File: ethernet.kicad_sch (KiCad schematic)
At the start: 41 parts, among them J10 J3011G21DNL, U3 LFSPXO025560REEL, U4 LAN8740A-EN

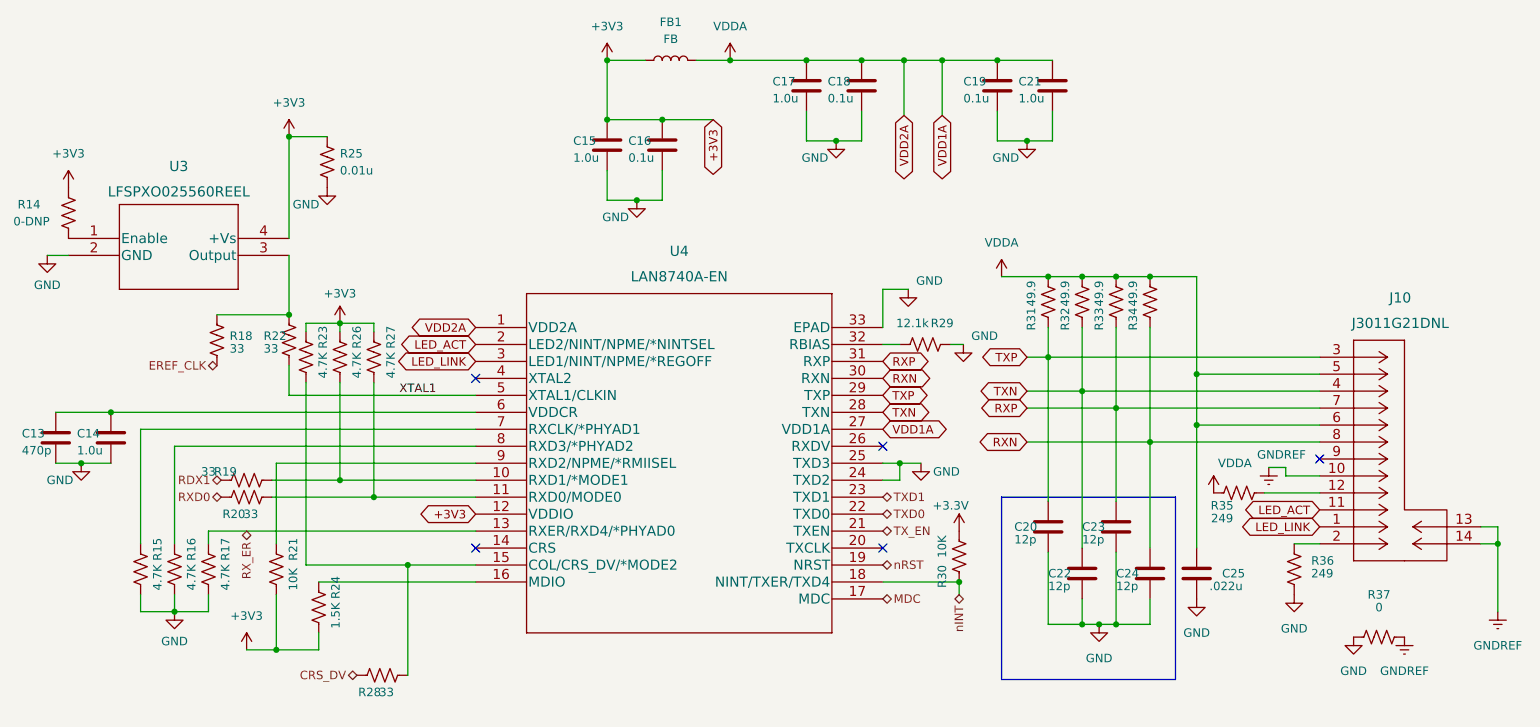
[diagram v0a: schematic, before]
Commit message: Imported AISLER 2Layer-Complex design rules Added Silkscreen to all passives to help with orientation Moved C15 and C16 to the back in order to be physically closer to the VDDIO pin of the LAN8740a Increased trace width of some 5v traces to the proper 0.5mm
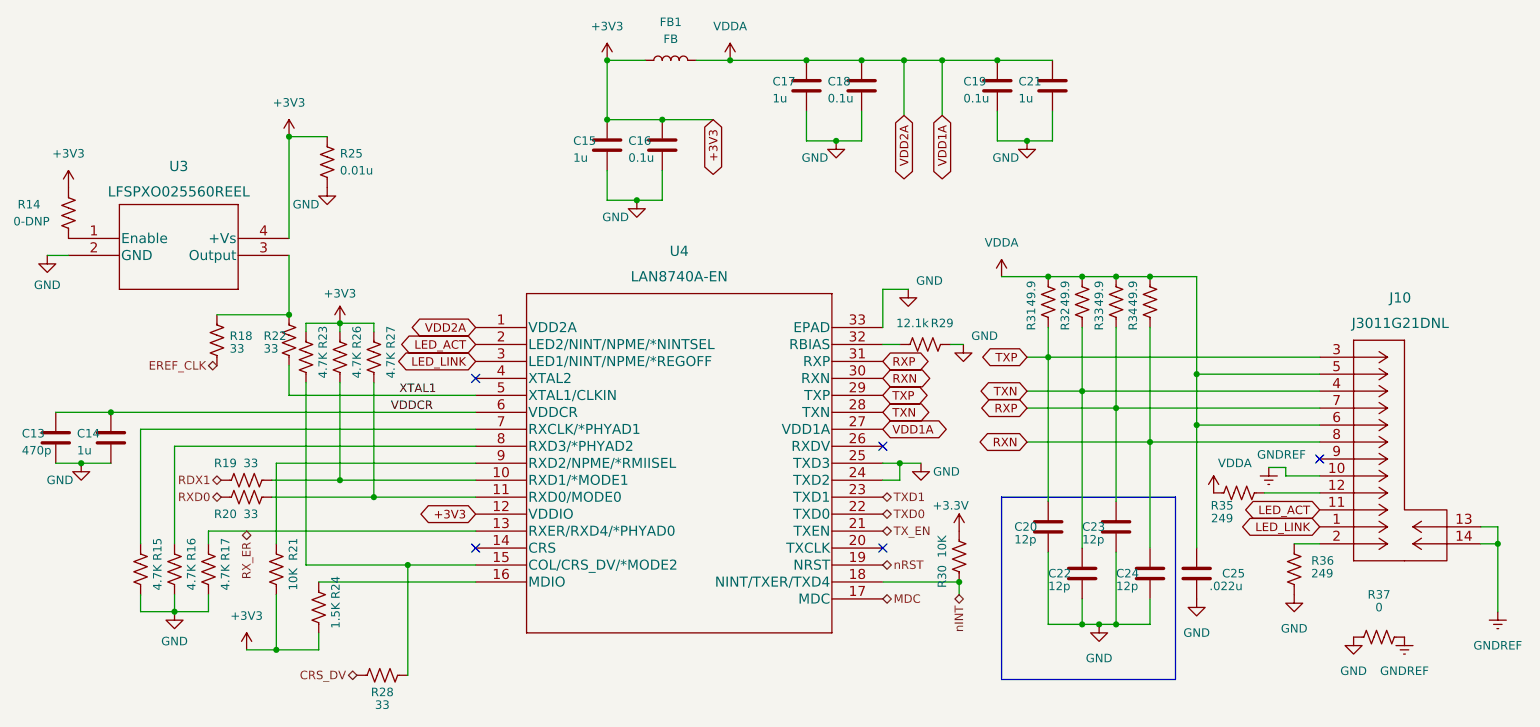
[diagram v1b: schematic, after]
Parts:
- C14, C15, C17, C21: value 1.0u -> 1u
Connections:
- net VDDCR: now reaches C13.1, C14.1, U4.6 (VDDCR)
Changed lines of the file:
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@@
     (stroke (width 0) (type default) (color 0 0 0 0))
+  )
+  (label "VDDCR" (at 80.01 85.09 0)
+    (effects (font (size 1.27 1.27)) (justify left bottom))
   )
   (label "XTAL1" (at 81.28 82.55 0)
@@
   (symbol (lib_id "Device:R_US") (at 58.42 97.79 270) (unit 1)
     (in_bom yes) (on_board yes)
-    (property "Reference" "R20" (id 0) (at 56.515 100.33 90))
+    (property "Reference" "R20" (id 0) (at 55.245 100.33 90))
     (property "Value" "33" (id 1) (at 59.055 100.33 90))
     (property "Footprint" "Lambley:0603-1608M" (id 2) (at 58.166 98.806 90)
@@
   (symbol (lib_id "Device:R_US") (at 58.42 95.25 270) (unit 1)
     (in_bom yes) (on_board yes)
-    (property "Reference" "R19" (id 0) (at 55.245 93.98 90))
-    (property "Value" "33" (id 1) (at 52.705 93.98 90))
+    (property "Reference" "R19" (id 0) (at 55.245 92.71 90))
+    (property "Value" "33" (id 1) (at 59.055 92.71 90))
     (property "Footprint" "Lambley:0603-1608M" (id 2) (at 58.166 96.266 90)
       (effects (font (size 1.27 1.27)) hide)
@@
       (effects (font (size 1.27 1.27)) (justify left))
     )
-    (property "Value" "1.0u" (id 1) (at 107.315 46.99 0)
+    (property "Value" "1u" (id 1) (at 107.315 46.99 0)
       (effects (font (size 1.27 1.27)) (justify left))
     )
@@
       (effects (font (size 1.27 1.27)) (justify left))
     )
-    (property "Value" "1.0u" (id 1) (at 137.16 38.1 0)
+    (property "Value" "1u" (id 1) (at 137.16 38.1 0)
       (effects (font (size 1.27 1.27)) (justify left))
     )
@@
       (effects (font (size 1.27 1.27)) (justify left))
     )
-    (property "Value" "1.0u" (id 1) (at 33.02 90.805 0)
+    (property "Value" "1u" (id 1) (at 33.02 90.805 0)
       (effects (font (size 1.27 1.27)) (justify left))
     )
@@
   (symbol (lib_id "Device:R_US") (at 78.74 124.46 270) (unit 1)
     (in_bom yes) (on_board yes)
-    (property "Reference" "R28" (id 0) (at 76.835 127 90))
-    (property "Value" "33" (id 1) (at 79.375 127 90))
+    (property "Reference" "R28" (id 0) (at 78.74 127 90))
+    (property "Value" "33" (id 1) (at 78.74 128.905 90))
     (property "Footprint" "Lambley:0603-1608M" (id 2) (at 78.486 125.476 90)
       (effects (font (size 1.27 1.27)) hide)
@@
       (effects (font (size 1.27 1.27)) (justify left))
     )
-    (property "Value" "1.0u" (id 1) (at 173.99 38.1 0)
-      (effects (font (size 1.27 1.27)) (justify left))
-    )
+    (property "Value" "1u" (id 1) (at 173.99 38.1 0)
+      (effects (font (size 1.27 1.27)) (justify left))
+    )

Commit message: Fixed nINT not actually being connected to 3v3 Changed the pic32MX7* 100 pin footprint from the T package to the F package Added some silkscreen around the DIGITAL and ANALOG headers
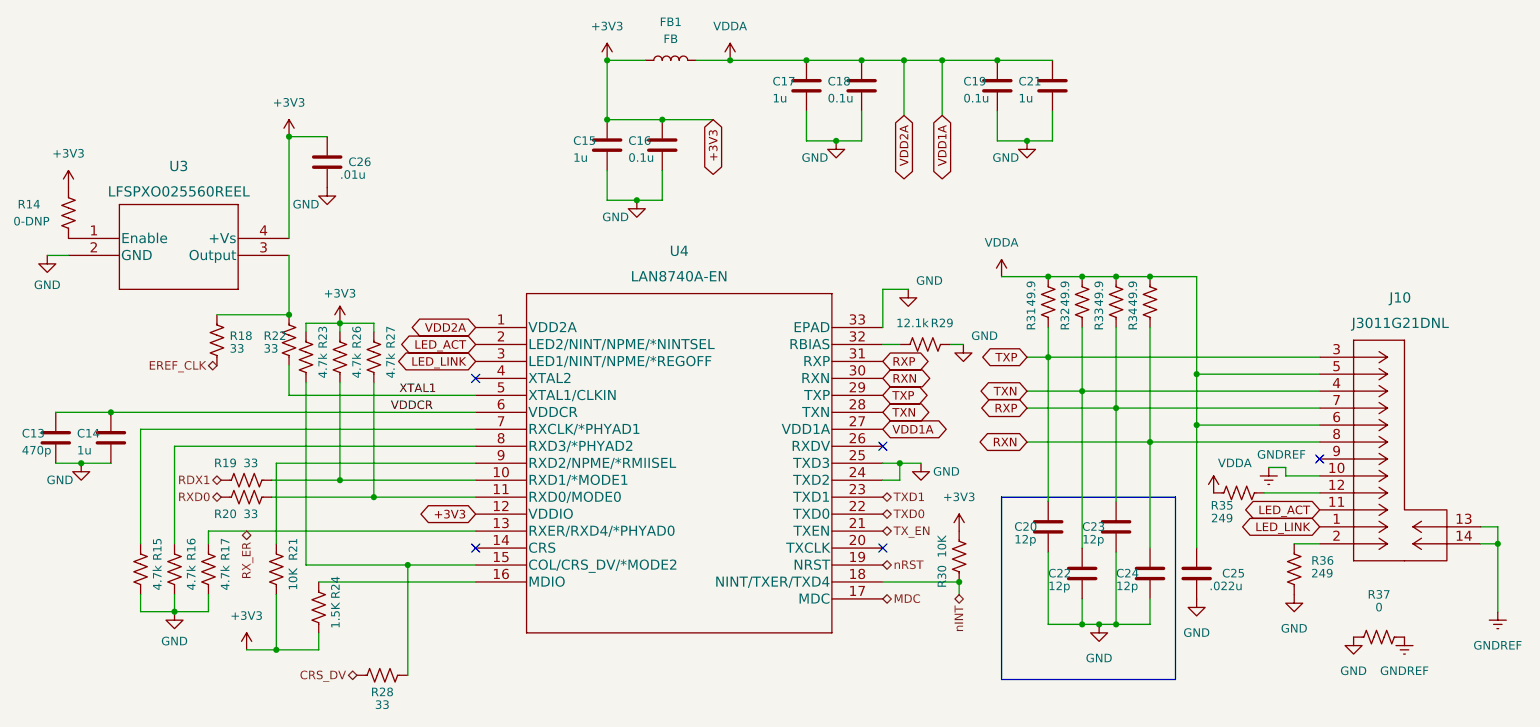
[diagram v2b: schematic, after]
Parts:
- removed R25: 0.01u, Lambley:0603-1608M, symbol Device:R_US
- added C26: .01u, Lambley:0603-1608M, symbol Device:C
- R15, R16, R17, R23, R26, R27: value 4.7K -> 4.7k
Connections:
- net +3.3V is gone; now on net +3V3: R30.1
- net +3V3: now also C26.1
- net GND: now also C26.2
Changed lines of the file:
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@@
     (pin "2")
-  )
-  (symbol (lib_id "power:+3.3V") (at 165.1 102.87 0) (unit 1)
-    (in_bom yes) (on_board yes)
-    (property "Reference" "#PWR0158" (id 0) (at 165.1 106.68 0)
-      (effects (font (size 1.27 1.27)) hide)
-    )
-    (property "Value" "+3.3V" (id 1) (at 163.83 99.06 0))
-    (property "Footprint" "" (id 2) (at 165.1 102.87 0)
-      (effects (font (size 1.27 1.27)) hide)
-    )
-    (property "Datasheet" "" (id 3) (at 165.1 102.87 0)
-      (effects (font (size 1.27 1.27)) hide)
-    )
-    (pin "1")
   )
   (symbol (lib_id "power:GND") (at 28.575 61.595 0) (unit 1)
@@
     (pin "1")
   )
-  (symbol (lib_id "Device:R_US") (at 70.485 47.625 180) (unit 1)
-    (in_bom yes) (on_board yes) (fields_autoplaced)
-    (property "Reference" "R25" (id 0) (at 72.39 46.3549 0)
-      (effects (font (size 1.27 1.27)) (justify right))
-    )
-    (property "Value" "0.01u" (id 1) (at 72.39 48.8949 0)
-      (effects (font (size 1.27 1.27)) (justify right))
-    )
-    (property "Footprint" "Lambley:0603-1608M" (id 2) (at 69.469 47.371 90)
-      (effects (font (size 1.27 1.27)) hide)
-    )
-    (property "Datasheet" "~" (id 3) (at 70.485 47.625 0)
-      (effects (font (size 1.27 1.27)) hide)
-    )
-    (pin "1")
-    (pin "2")
-  )
   (symbol (lib_id "power:GND") (at 165.735 74.93 0) (unit 1)
     (in_bom yes) (on_board yes)
@@
       (effects (font (size 1.27 1.27)) (justify right))
     )
-    (property "Value" "4.7K" (id 1) (at 50.165 111.76 90)
+    (property "Value" "4.7k" (id 1) (at 50.165 111.76 90)
       (effects (font (size 1.27 1.27)) (justify right))
     )
@@
       (effects (font (size 1.27 1.27)) (justify right))
     )
-    (property "Value" "4.7K" (id 1) (at 45.085 111.76 90)
+    (property "Value" "4.7k" (id 1) (at 45.085 111.76 90)
       (effects (font (size 1.27 1.27)) (justify right))
     )
@@
       (effects (font (size 1.27 1.27)) (justify right))
     )
-    (property "Value" "4.7K" (id 1) (at 69.85 80.01 90)
+    (property "Value" "4.7k" (id 1) (at 69.85 80.01 90)
       (effects (font (size 1.27 1.27)) (justify right))
     )
@@
     (pin "1")
   )
+  (symbol (lib_id "power:+3V3") (at 165.1 102.87 0) (unit 1)
+    (in_bom yes) (on_board yes) (fields_autoplaced)
+    (property "Reference" "#PWR0158" (id 0) (at 165.1 106.68 0)
+      (effects (font (size 1.27 1.27)) hide)
+    )
+    (property "Value" "+3V3" (id 1) (at 165.1 97.79 0))
+    (property "Footprint" "" (id 2) (at 165.1 102.87 0)
+      (effects (font (size 1.27 1.27)) hide)
+    )
+    (property "Datasheet" "" (id 3) (at 165.1 102.87 0)
+      (effects (font (size 1.27 1.27)) hide)
+    )
+    (pin "1")
+  )
   (symbol (lib_id "Device:C") (at 150.495 36.195 0) (unit 1)
     (in_bom yes) (on_board yes)
@@
       (effects (font (size 1.27 1.27)) (justify right))
     )
-    (property "Value" "4.7K" (id 1) (at 74.93 80.01 90)
+    (property "Value" "4.7k" (id 1) (at 74.93 80.01 90)
       (effects (font (size 1.27 1.27)) (justify right))
     )
@@
     (pin "2")
   )
+  (symbol (lib_id "Device:C") (at 70.485 47.625 0) (unit 1)
+    (in_bom yes) (on_board yes)
+    (property "Reference" "C26" (id 0) (at 73.66 47.625 0)
+      (effects (font (size 1.27 1.27)) (justify left))
+    )
+    (property "Value" ".01u" (id 1) (at 72.39 49.53 0)
+      (effects (font (size 1.27 1.27)) (justify left))
+    )
+    (property "Footprint" "Lambley:0603-1608M" (id 2) (at 71.4502 51.435 0)
+      (effects (font (size 1.27 1.27)) hide)
+    )
+    (property "Datasheet" "~" (id 3) (at 70.485 47.625 0)
+      (effects (font (size 1.27 1.27)) hide)
+    )
+    (pin "1")
+    (pin "2")
+  )
   (symbol (lib_id "Device:R_US") (at 77.47 76.835 180) (unit 1)
     (in_bom yes) (on_board yes)
@@
       (effects (font (size 1.27 1.27)) (justify right))
     )
-    (property "Value" "4.7K" (id 1) (at 80.01 80.01 90)
+    (property "Value" "4.7k" (id 1) (at 80.01 80.01 90)
       (effects (font (size 1.27 1.27)) (justify right))
     )
@@
       (effects (font (size 1.27 1.27)) (justify right))
     )
-    (property "Value" "4.7K" (id 1) (at 55.245 111.76 90)
-      (effects (font (size 1.27 1.27)) (justify right))
-    )
+    (property "Value" "4.7k" (id 1) (at 55.245 111.76 90)
+      (effects (font (size 1.27 1.27)) (justify right))
+    )

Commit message: Added connection for MDIO to the PIC Complete redesign of board, reduced size from 100x50 to 75x35mm Readded C15 and C16 to the front Added some test points
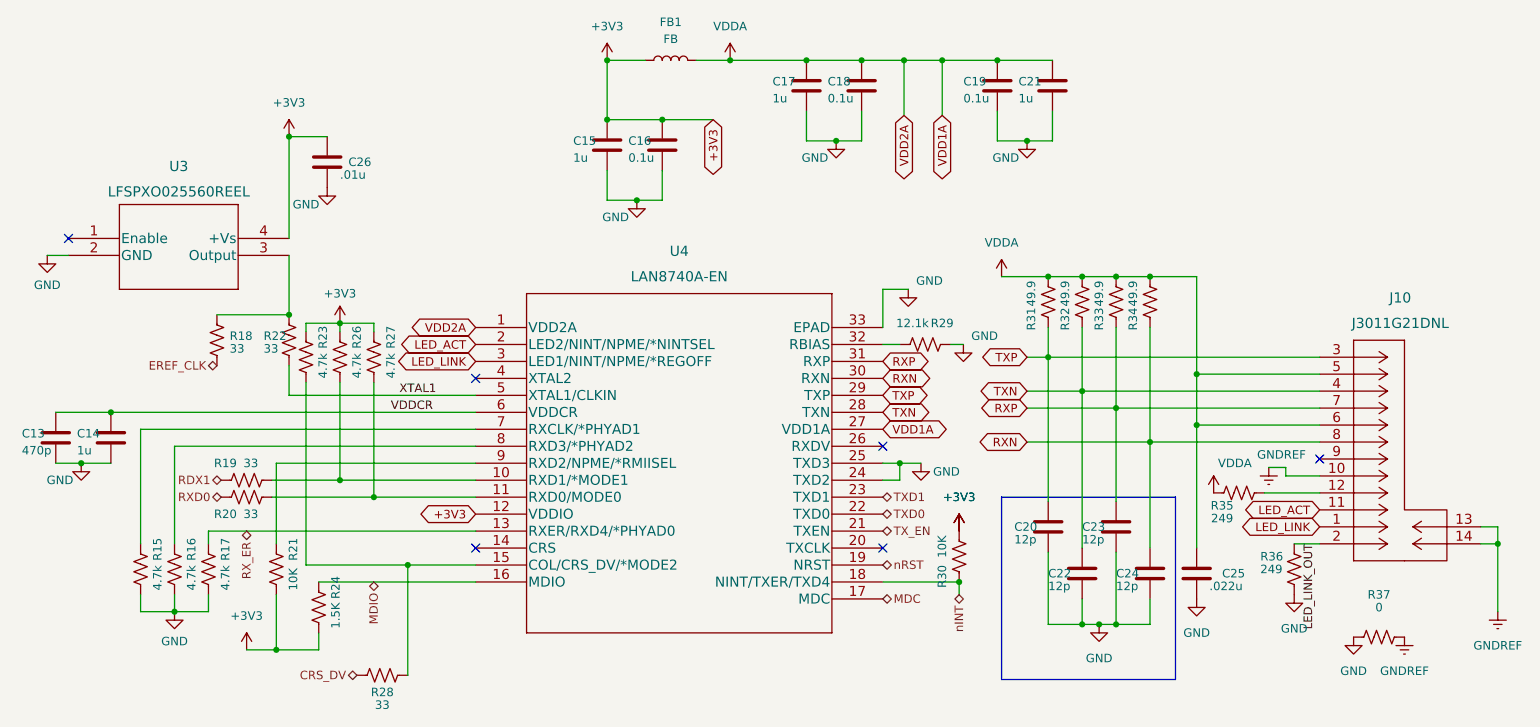
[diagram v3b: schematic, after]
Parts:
- removed R14: 0-DNP, Lambley:0603-1608M, symbol Device:R_US
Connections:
- net MDIO: now reaches R24.2, U4.16 (MDIO)
- net LED_LINK_OUT: now reaches J10.2, R36.1
- no-connect marks 5 -> 6
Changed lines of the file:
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@@
   (junction (at 245.745 104.775) (diameter 0) (color 0 0 0 0)
   )
+  (no_connect (at 31.75 59.055))
   (no_connect (at 153.67 90.17))
   (no_connect (at 153.67 105.41))
@@
     (stroke (width 0) (type default) (color 0 0 0 0))
   )
+  (wire (pts (xy 215.265 104.775) (xy 219.075 104.775))
+    (stroke (width 0) (type default) (color 0 0 0 0))
+  )
   (wire (pts (xy 183.515 64.77) (xy 188.595 64.77))
     (stroke (width 0) (type default) (color 0 0 0 0))
@@
     (stroke (width 0) (type default) (color 0 0 0 0))
   )
-  (wire (pts (xy 215.265 104.775) (xy 219.075 104.775))
-    (stroke (width 0) (type default) (color 0 0 0 0))
-  )
   (polyline (pts (xy 171.45 97.79) (xy 171.45 125.095))
     (stroke (width 0) (type default) (color 0 0 0 0))
@@
   (wire (pts (xy 183.515 72.39) (xy 183.515 81.915))
     (stroke (width 0) (type default) (color 0 0 0 0))
+  )
+  (label "LED_LINK_OUT" (at 218.44 104.775 270)
+    (effects (font (size 1.27 1.27)) (justify right bottom))
   )
   (label "VDDCR" (at 80.01 85.09 0)
@@
   )
   (hierarchical_label "RXD0" (shape bidirectional) (at 54.61 97.79 180)
+    (effects (font (size 1.27 1.27)) (justify right))
+  )
+  (hierarchical_label "MDIO" (shape bidirectional) (at 77.47 110.49 270)
     (effects (font (size 1.27 1.27)) (justify right))
   )
@@
     (pin "2")
   )
-  (symbol (lib_id "power:+3V3") (at 31.75 51.435 0) (unit 1)
-    (in_bom yes) (on_board yes) (fields_autoplaced)
-    (property "Reference" "#PWR0163" (id 0) (at 31.75 55.245 0)
-      (effects (font (size 1.27 1.27)) hide)
-    )
-    (property "Value" "+3V3" (id 1) (at 31.75 46.355 0))
-    (property "Footprint" "" (id 2) (at 31.75 51.435 0)
-      (effects (font (size 1.27 1.27)) hide)
-    )
-    (property "Datasheet" "" (id 3) (at 31.75 51.435 0)
-      (effects (font (size 1.27 1.27)) hide)
-    )
-    (pin "1")
-  )
   (symbol (lib_id "power:GND") (at 186.055 116.84 0) (unit 1)
     (in_bom yes) (on_board yes) (fields_autoplaced)
@@
   (symbol (lib_id "Device:R_US") (at 215.265 108.585 0) (unit 1)
     (in_bom yes) (on_board yes)
-    (property "Reference" "R36" (id 0) (at 217.805 107.3149 0)
-      (effects (font (size 1.27 1.27)) (justify left))
-    )
-    (property "Value" "249" (id 1) (at 217.805 109.22 0)
+    (property "Reference" "R36" (id 0) (at 210.185 106.6799 0)
+      (effects (font (size 1.27 1.27)) (justify left))
+    )
+    (property "Value" "249" (id 1) (at 210.185 108.585 0)
       (effects (font (size 1.27 1.27)) (justify left))
     )
@@
     )
     (property "Datasheet" "~" (id 3) (at 215.265 108.585 0)
-      (effects (font (size 1.27 1.27)) hide)
-    )
-    (pin "1")
-    (pin "2")
-  )
-  (symbol (lib_id "Device:R_US") (at 31.75 55.245 180) (unit 1)
-    (in_bom yes) (on_board yes)
-    (property "Reference" "R14" (id 0) (at 24.13 53.975 0)
-      (effects (font (size 1.27 1.27)) (justify right))
-    )
-    (property "Value" "0-DNP" (id 1) (at 23.495 56.515 0)
-      (effects (font (size 1.27 1.27)) (justify right))
-    )
-    (property "Footprint" "Lambley:0603-1608M" (id 2) (at 30.734 54.991 90)
-      (effects (font (size 1.27 1.27)) hide)
-    )
-    (property "Datasheet" "~" (id 3) (at 31.75 55.245 0)
       (effects (font (size 1.27 1.27)) hide)
     )
@@
     (pin "2")
   )
+  (symbol (lib_id "power:+3V3") (at 165.1 102.87 0) (unit 1)
+    (in_bom yes) (on_board yes) (fields_autoplaced)
+    (property "Reference" "#PWR0158" (id 0) (at 165.1 106.68 0)
+      (effects (font (size 1.27 1.27)) hide)
+    )
+    (property "Value" "+3V3" (id 1) (at 165.1 97.79 0))
+    (property "Footprint" "" (id 2) (at 165.1 102.87 0)
+      (effects (font (size 1.27 1.27)) hide)
+    )
+    (property "Datasheet" "" (id 3) (at 165.1 102.87 0)
+      (effects (font (size 1.27 1.27)) hide)
+    )
+    (pin "1")
+  )
   (symbol (lib_id "power:+3V3") (at 64.77 43.815 0) (unit 1)
